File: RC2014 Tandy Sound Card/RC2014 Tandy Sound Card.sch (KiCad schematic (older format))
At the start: 8 parts, among them J1 CONN_01X39, J2 Sound, U1 74LS138, U2 74LS245, U3 SN76489AN

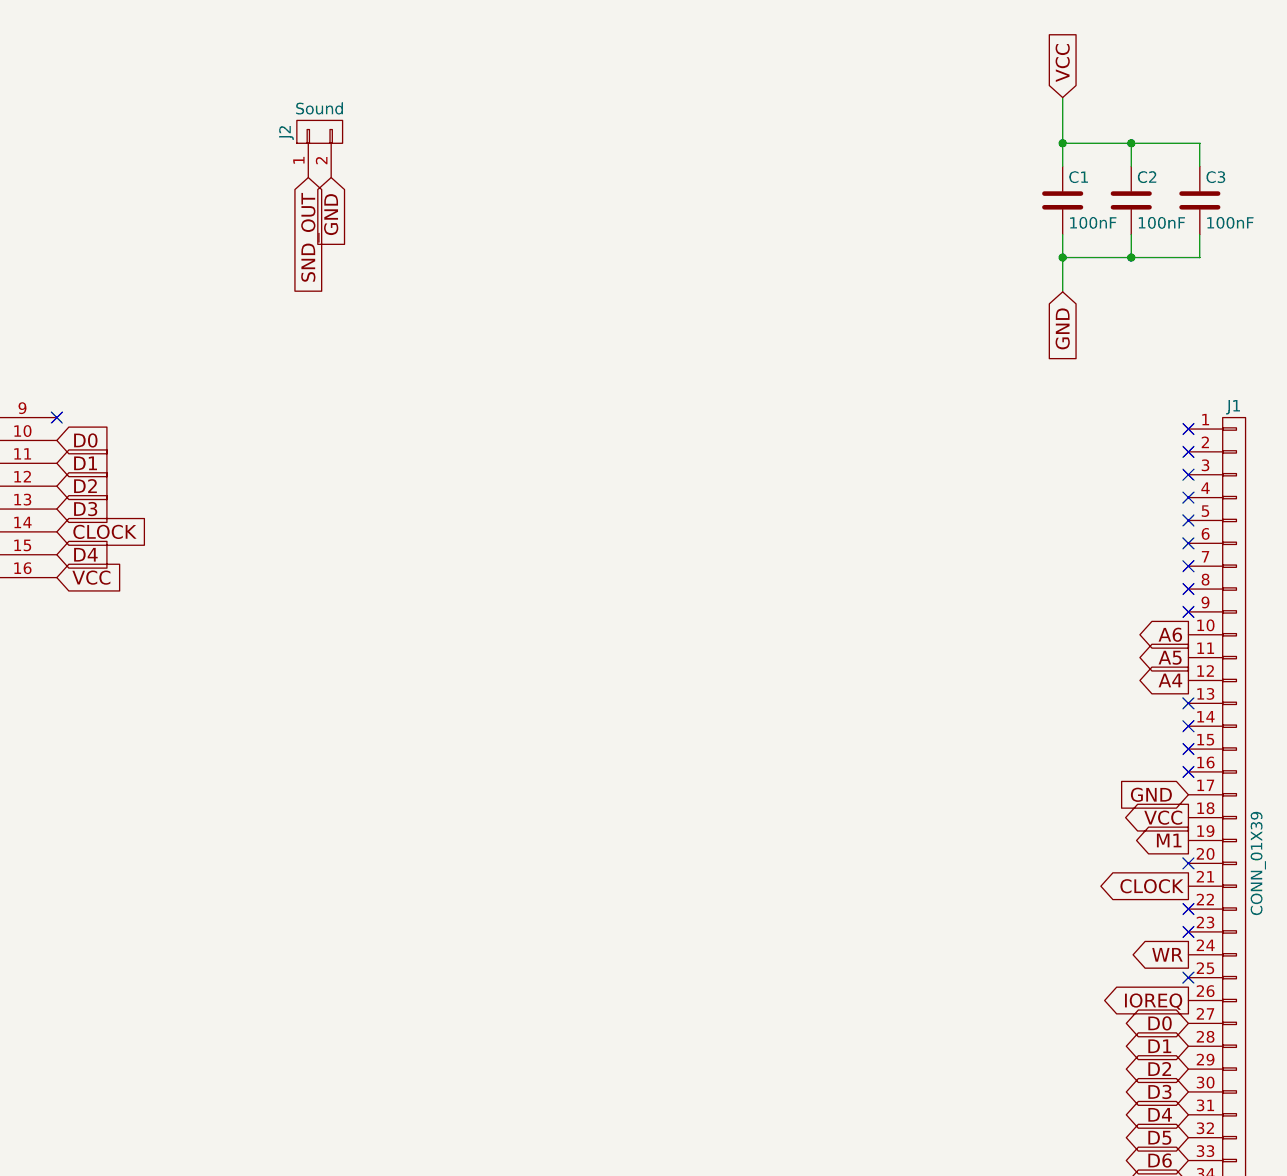
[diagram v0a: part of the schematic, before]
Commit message: Added TDA7065A audio amplification
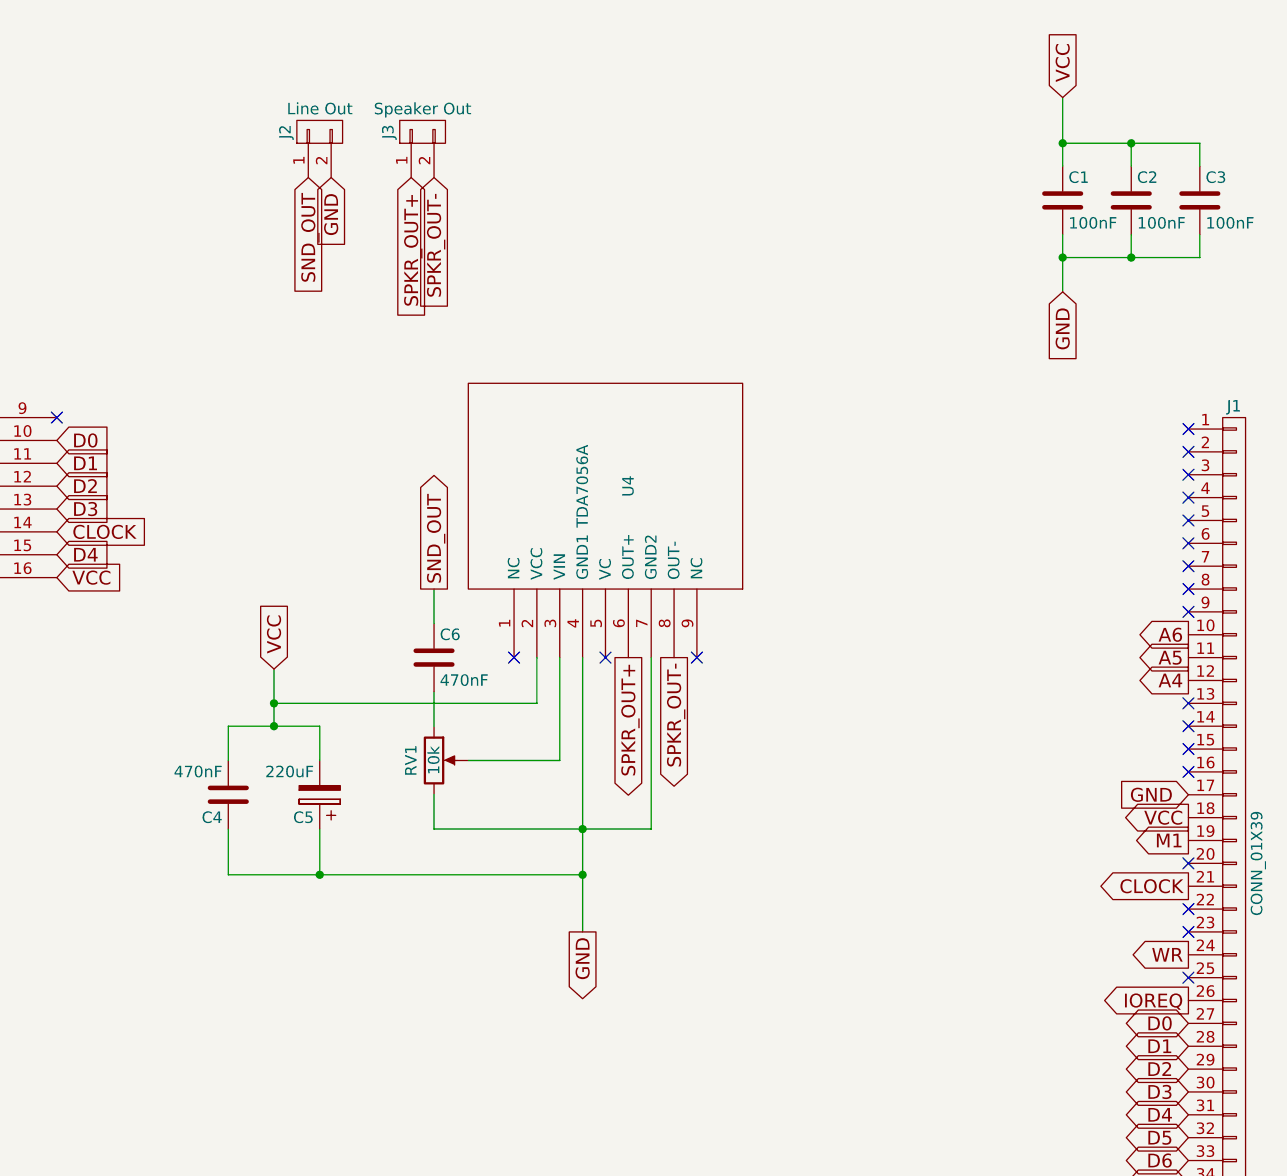
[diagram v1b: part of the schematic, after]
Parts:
- added C4, C6: 470nF, Capacitors_THT:C_Disc_D4.7mm_W2.5mm_P5.00mm, symbol C
- added C5: 220uF, Capacitors_THT:CP_Radial_D5.0mm_P2.00mm, symbol CP
- added J3: Speaker Out, Pin_Headers:Pin_Header_Angled_1x02_Pitch2.54mm, symbol CONN_01X02
- added RV1: 10k, Potentiometers:Potentiometer_Trimmer_Bourns_3296W, symbol POT
- added U4: TDA7056A, Pin_Headers:Pin_Header_Straight_1x09_Pitch2.54mm, symbol TDA7056A
- J2: value Sound -> Line Out
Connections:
- net GND: now also C4.1, C5.1, RV1.3, U4.4 (GND1), U4.7 (GND2)
- net SND_OUT: now also C6.1
- net VCC: now also C4.2, C5.2, U4.2 (VCC)
- new net: RV1.2, U4.3 (VIN)
- new net: C6.2, RV1.1
- new net SPKR_OUT+: J3.1 (P1), U4.6 (OUT+)
- new net SPKR_OUT-: J3.2 (P2), U4.8 (OUT-)
- no-connect marks 30 -> 33
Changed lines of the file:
@@
 LIBS:valves
 LIBS:SN76489AN
+LIBS:TDA7056A
 LIBS:RC2014 Tandy Sound Card-cache
 EELAYER 25 0
@@
 NoConn ~ 3800 1800
 NoConn ~ 10600 4500
-Wire Wire Line
-	10050 850  10050 1150
-Wire Wire Line
-	10050 1450 10050 1700
 NoConn ~ 10600 3100
 NoConn ~ 10600 3000
@@
 Text GLabel 1950 3450 0    60   Output ~ 0
 GND
-Wire Wire Line
-	3350 2550 4150 2550
-Wire Wire Line
-	3350 2650 3550 2650
-Wire Wire Line
-	3550 2650 3550 3600
-Wire Wire Line
-	3350 2750 3550 2750
-Connection ~ 3550 2750
-Wire Wire Line
-	3350 2850 3550 2850
-Connection ~ 3550 2850
-Wire Wire Line
-	3350 2950 4150 2950
-Connection ~ 3550 2950
-Wire Wire Line
-	3350 3050 3550 3050
-Connection ~ 3550 3050
-Wire Wire Line
-	3350 3150 3550 3150
-Connection ~ 3550 3150
-Wire Wire Line
-	3350 3250 3550 3250
-Connection ~ 3550 3250
-Wire Wire Line
-	3200 1400 3800 1400
 Text GLabel 3550 3600 3    60   Output ~ 0
 GND
@@
 WR
 NoConn ~ 3800 1400
-Wire Wire Line
-	3800 1300 3200 1300
-Wire Wire Line
-	3800 1200 3200 1200
-Wire Wire Line
-	3800 1500 3200 1500
-Wire Wire Line
-	3800 1600 3200 1600
-Wire Wire Line
-	3800 1700 3200 1700
-Wire Wire Line
-	3800 1800 3200 1800
-Wire Wire Line
-	3800 1100 3200 1100
 Text Label 3150 1500 0    60   ~ 0
 Port0_RD
@@
 Text GLabel 1700 3700 3    60   Input ~ 0
 PORT32_RD
-Wire Wire Line
-	1700 3700 1700 3550
-Wire Wire Line
-	1700 3550 1950 3550
-Wire Wire Line
-	4000 2650 4000 3250
-Wire Wire Line
-	4000 2650 4150 2650
-Wire Wire Line
-	4150 2750 4000 2750
-Connection ~ 4000 2750
 Text GLabel 4150 3250 3    60   Output ~ 0
 SND_OUT
-Wire Wire Line
-	4150 2850 4150 3250
 $Comp
 L C C2
@@
 	1    0    0    -1
 $EndComp
-Wire Wire Line
-	10050 1050 10650 1050
-Wire Wire Line
-	10650 1050 10650 1150
-Connection ~ 10050 1050
-Wire Wire Line
-	10650 1450 10650 1550
-Wire Wire Line
-	10650 1550 10050 1550
-Connection ~ 10050 1550
-Wire Wire Line
-	10350 1450 10350 1550
-Connection ~ 10350 1550
-Wire Wire Line
-	10350 1150 10350 1050
-Connection ~ 10350 1050
 $Comp
 L CONN_01X02 J2
@@
 P 6800 1000
 F 0 "J2" H 6800 1150 50  0000 C CNN
-F 1 "Sound" V 6900 1000 50  0000 C CNN
+F 1 "Line Out" V 6900 1000 50  0000 C CNN
 F 2 "Pin_Headers:Pin_Header_Angled_1x02_Pitch2.54mm" H 6800 1000 50  0001 C CNN
 F 3 "" H 6800 1000 50  0001 C CNN
@@
 NoConn ~ 10600 4200
 NoConn ~ 10600 4700
+$Comp
+L TDA7056A U4
+U 1 1 5917EAD4
+P 8050 2550
+F 0 "U4" H 8050 2450 50  0000 C CNN
+F 1 "TDA7056A" H 8050 2650 50  0000 C CNN
+F 2 "Pin_Headers:Pin_Header_Straight_1x09_Pitch2.54mm" H 8050 2550 50  0001 C CNN
+F 3 "DOCUMENTATION" H 8050 2550 50  0001 C CNN
+	1    8050 2550
+	0    -1   -1   0
+$EndComp
+$Comp
+L CONN_01X02 J3
+U 1 1 5917F160
+P 7250 1000
+F 0 "J3" H 7250 1150 50  0000 C CNN
+F 1 "Speaker Out" V 7350 1000 50  0000 C CNN
+F 2 "Pin_Headers:Pin_Header_Angled_1x02_Pitch2.54mm" H 7250 1000 50  0001 C CNN
+F 3 "" H 7250 1000 50  0001 C CNN
+	1    7250 1000
+	0    -1   -1   0
+$EndComp
+Text GLabel 7950 4500 3    60   Output ~ 0
+GND
+Text GLabel 7200 1200 3    60   Input ~ 0
+SPKR_OUT+
+Text GLabel 7300 1200 3    60   Input ~ 0
+SPKR_OUT-
+Text GLabel 8150 3300 3    60   Output ~ 0
+SPKR_OUT+
+Text GLabel 8350 3300 3    60   Output ~ 0
+SPKR_OUT-
+Text GLabel 6600 3350 1    60   Input ~ 0
+VCC
+NoConn ~ 7650 3300
+NoConn ~ 8450 3300
+$Comp
+L C C6
+U 1 1 591812F7
+P 7300 3300
+F 0 "C6" H 7325 3400 50  0000 L CNN
+F 1 "470nF" H 7325 3200 50  0000 L CNN
+F 2 "Capacitors_THT:C_Disc_D4.7mm_W2.5mm_P5.00mm" H 7338 3150 50  0001 C CNN
+F 3 "" H 7300 3300 50  0001 C CNN
+	1    7300 3300
+	1    0    0    -1
+$EndComp
+$Comp
+L POT RV1
+U 1 1 591821C0
+P 7300 3750
+F 0 "RV1" V 7200 3750 50  0000 C CNN
+F 1 "10k" V 7300 3750 50  0000 C CNN
+F 2 "Potentiometers:Potentiometer_Trimmer_Bourns_3296W" H 7300 3750 50  0001 C CNN
+F 3 "" H 7300 3750 50  0001 C CNN
+	1    7300 3750
+	1    0    0    -1
+$EndComp
+Text GLabel 7300 3000 1    60   Output ~ 0
+SND_OUT
+$Comp
+L C C4
+U 1 1 59182F48
+P 6400 3900
+F 0 "C4" H 6425 4000 50  0000 L CNN
+F 1 "470nF" H 6425 3800 50  0000 L CNN
+F 2 "Capacitors_THT:C_Disc_D4.7mm_W2.5mm_P5.00mm" H 6438 3750 50  0001 C CNN
+F 3 "" H 6400 3900 50  0001 C CNN
+	1    6400 3900
+	-1   0    0    1
+$EndComp
+$Comp
+L CP C5
+U 1 1 59182FE8
+P 6800 3900
+F 0 "C5" H 6825 4000 50  0000 L CNN
+F 1 "220uF" H 6825 3800 50  0000 L CNN
+F 2 "Capacitors_THT:CP_Radial_D5.0mm_P2.00mm" H 6838 3750 50  0001 C CNN
+F 3 "" H 6800 3900 50  0001 C CNN
+	1    6800 3900
+	-1   0    0    1
+$EndComp
+Wire Wire Line
+	10050 850  10050 1150
+Wire Wire Line
+	10050 1450 10050 1700
+Wire Wire Line
+	3350 2550 4150 2550
+Wire Wire Line
+	3350 2650 3550 2650
+Wire Wire Line
+	3550 2650 3550 3600
+Wire Wire Line
+	3350 2750 3550 2750
+Connection ~ 3550 2750
+Wire Wire Line
+	3350 2850 3550 2850
+Connection ~ 3550 2850
+Wire Wire Line
+	3350 2950 4150 2950
+Connection ~ 3550 2950
+Wire Wire Line
+	3350 3050 3550 3050
+Connection ~ 3550 3050
+Wire Wire Line
+	3350 3150 3550 3150
+Connection ~ 3550 3150
+Wire Wire Line
+	3350 3250 3550 3250
+Connection ~ 3550 3250
+Wire Wire Line
+	3200 1400 3800 1400
+Wire Wire Line
+	3800 1300 3200 1300
+Wire Wire Line
+	3800 1200 3200 1200
+Wire Wire Line
+	3800 1500 3200 1500
+Wire Wire Line
+	3800 1600 3200 1600
+Wire Wire Line
+	3800 1700 3200 1700
+Wire Wire Line
+	3800 1800 3200 1800
+Wire Wire Line
+	3800 1100 3200 1100
+Wire Wire Line
+	1700 3700 1700 3550
+Wire Wire Line
+	1700 3550 1950 3550
+Wire Wire Line
+	4000 2650 4000 3250
+Wire Wire Line
+	4000 2650 4150 2650
+Wire Wire Line
+	4150 2750 4000 2750
+Connection ~ 4000 2750
+Wire Wire Line
+	4150 2850 4150 3250
+Wire Wire Line
+	10050 1050 10650 1050
+Wire Wire Line
+	10650 1050 10650 1150
+Connection ~ 10050 1050
+Wire Wire Line
+	10650 1550 10650 1450
+Wire Wire Line
+	10050 1550 10650 1550
+Connection ~ 10050 1550
+Wire Wire Line
+	10350 1450 10350 1550
+Connection ~ 10350 1550
+Wire Wire Line
+	10350 1150 10350 1050
+Connection ~ 10350 1050
+Wire Wire Line
+	7950 3300 7950 4500
+Wire Wire Line
+	8250 4050 8250 3300
+Wire Wire Line
+	7300 4050 8250 4050
+Connection ~ 7950 4050
+Wire Wire Line
+	7450 3750 7850 3750
+Wire Wire Line
+	7850 3750 7850 3300
+Wire Wire Line
+	7300 3000 7300 3150
+Wire Wire Line
+	7300 3450 7300 3600
+Wire Wire Line
+	7300 3900 7300 4050
+Wire Wire Line
+	6600 3500 7750 3500
+Wire Wire Line
+	7750 3500 7750 3300
+Wire Wire Line
+	6400 3600 6800 3600
+Wire Wire Line
+	6800 3600 6800 3750
+Wire Wire Line
+	6400 4250 7950 4250
+Wire Wire Line
+	6800 4250 6800 4050
+Connection ~ 7950 4250
+Connection ~ 6800 4250
+Wire Wire Line
+	6400 3600 6400 3750
+Wire Wire Line
+	6400 4050 6400 4250
+Wire Wire Line
+	6600 3350 6600 3600
+Connection ~ 6600 3600
+Connection ~ 6600 3500
+NoConn ~ 8050 3300
 $EndSCHEMATC
